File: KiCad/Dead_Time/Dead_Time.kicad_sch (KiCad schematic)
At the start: 13 parts, among them Q7 PNP_BC558, U1 L272M, U2 74AUC2G04

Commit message: alla pcber er klar til routing
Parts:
- removed U1: L272M, Package_DIP:DIP-8_W7.62mm_LongPads, symbol Amplifier_Operational:L272M
- removed U2: 74AUC2G04, Package_DIP:DIP-14_W7.62mm, symbol 74xGxx:74AUC2G04
- added U1: 74AUC2G04, Package_DIP:DIP-14_W7.62mm, symbol 74xGxx:74AUC2G04
- added U2: Opamp_Dual, Package_DIP:DIP-8_W7.62mm, symbol Device:Opamp_Dual
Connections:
- net +5V: now also U1.5 (VCC)
- net GND: now also U1.2 (GND)
- net Meas_VStep1: now also U2.2 (-)
- net Meas_VStep2: now also U2.5 (+)
- net PWM1: now also U1.1, U2.1
- net PWM1_NOT: now also U1.6
- net PWM2: now also U1.3, U2.7
- net PWM2_NOT: now also U1.4
- net at C3.1, R9.2: now also U2.3 (+), U2.6 (-)

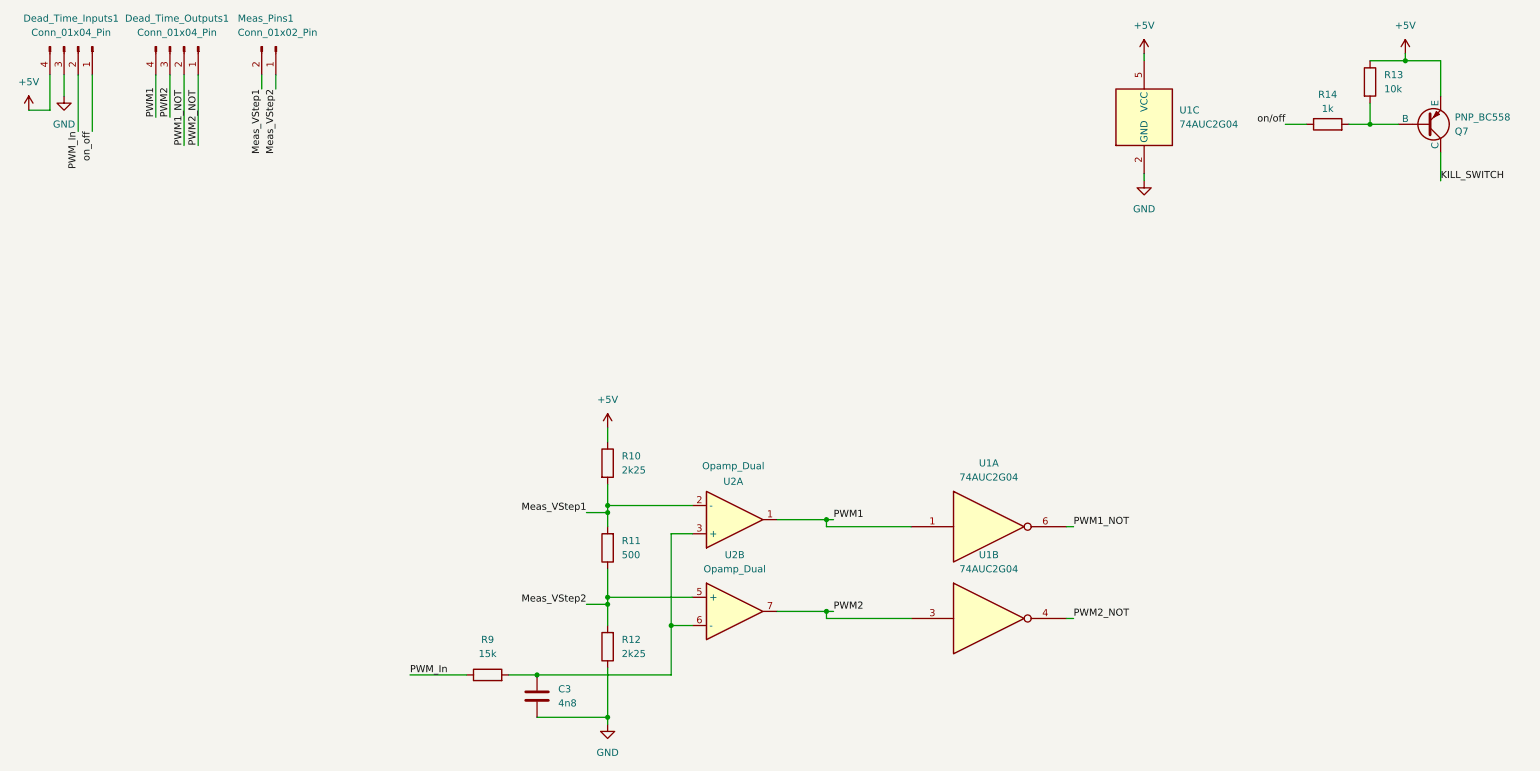
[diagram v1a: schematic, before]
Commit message: deadtime pcb almost done, missing 1 gnd connection
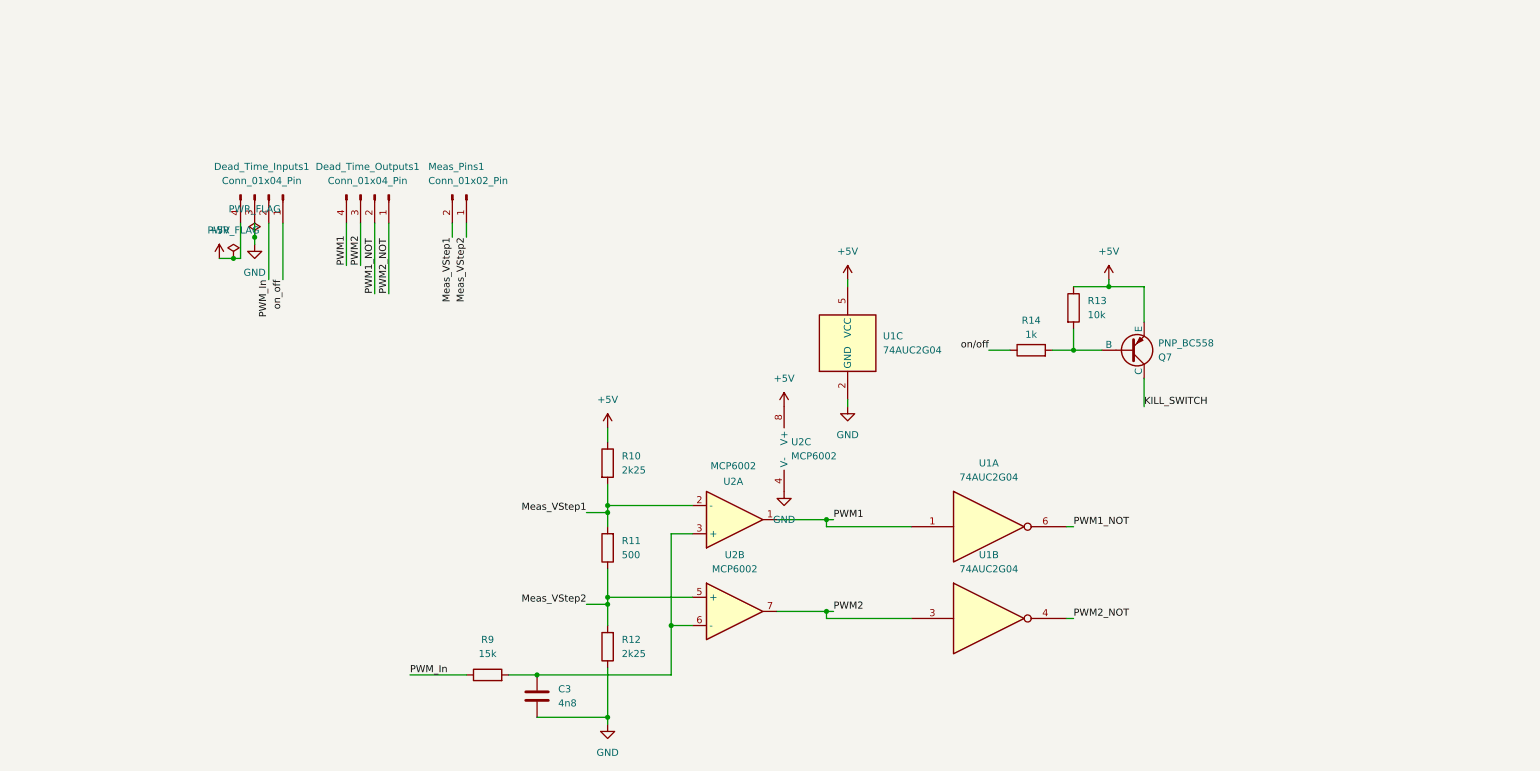
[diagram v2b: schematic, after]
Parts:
- added unit 3 of U2
- U2: value Opamp_Dual -> MCP6002
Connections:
- net +5V: now also U2.8 (V+)
- net GND: now also U2.4 (V-)
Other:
- moved on the sheet: Dead_Time_Inputs1, Dead_Time_Outputs1, Meas_Pins1, Q7, R13, R14, U1C

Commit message: gemme punkt før jeg laver om i deadtime pcb
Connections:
- net +5V: no longer U2.8 (V+)
- net KILL_SWITCH: now also U2.8 (V+)
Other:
- moved on the sheet: Dead_Time_Inputs1, Dead_Time_Outputs1, Meas_Pins1, Q7, R13, R14, U1C, U2C

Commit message: pcb layouts done
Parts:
- removed Meas_Pins1: Conn_01x02_Pin, Connector_PinHeader_2.54mm:PinHeader_1x02_P2.54mm_Vertical, symbol Connector:Conn_01x02_Pin
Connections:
- net Meas_VStep1: no longer names the net of R10.2, R11.2, U2.2 (-)
- net Meas_VStep2: no longer names the net of R11.1, R12.2, U2.5 (+)
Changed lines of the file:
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@@
 	(paper "A4")
-	(junction
-		(at 118.11 102.87)
-		(diameter 0)
-		(color 0 0 0 0)
-	)
 	(junction
 		(at 118.11 118.11)
@@
 	)
 	(junction
-		(at 118.11 119.38)
-		(diameter 0)
-		(color 0 0 0 0)
-	)
-	(junction
 		(at 256.54 31.75)
 		(diameter 0)
@@
 	(wire
 		(pts
-			(xy 114.3 119.38) (xy 118.11 119.38)
-		)
-		(stroke
-			(width 0)
-			(type default)
-		)
-	)
-	(wire
-		(pts
 			(xy 200.66 105.41) (xy 201.93 105.41)
 		)
@@
 	(wire
 		(pts
-			(xy 118.11 102.87) (xy 118.11 105.41)
+			(xy 118.11 101.6) (xy 118.11 105.41)
 		)
 		(stroke
@@
 	(wire
 		(pts
-			(xy 114.3 102.87) (xy 118.11 102.87)
-		)
-		(stroke
-			(width 0)
-			(type default)
-		)
-	)
-	(wire
-		(pts
 			(xy 200.66 121.92) (xy 201.93 121.92)
 		)
@@
 	(wire
 		(pts
-			(xy 68.58 24.13) (xy 68.58 26.67)
-		)
-		(stroke
-			(width 0)
-			(type default)
-		)
-	)
-	(wire
-		(pts
 			(xy 82.55 132.08) (xy 92.71 132.08)
 		)
@@
 	(wire
 		(pts
-			(xy 66.04 24.13) (xy 66.04 26.67)
-		)
-		(stroke
-			(width 0)
-			(type default)
-		)
-	)
-	(wire
-		(pts
 			(xy 105.41 132.08) (xy 129.54 132.08)
 		)
@@
 	(wire
 		(pts
-			(xy 118.11 101.6) (xy 118.11 102.87)
-		)
-		(stroke
-			(width 0)
-			(type default)
-		)
-	)
-	(wire
-		(pts
 			(xy 256.54 31.75) (xy 256.54 27.94)
 		)
@@
 	(wire
 		(pts
-			(xy 118.11 118.11) (xy 118.11 119.38)
-		)
-		(stroke
-			(width 0)
-			(type default)
-		)
-	)
-	(wire
-		(pts
 			(xy 262.89 19.05) (xy 262.89 20.32)
 		)
@@
 	(wire
 		(pts
-			(xy 118.11 119.38) (xy 118.11 123.19)
+			(xy 118.11 118.11) (xy 118.11 123.19)
 		)
 		(stroke
@@
 		)
 	)
-	(label "Meas_VStep1"
-		(at 66.04 26.67 270)
-		(effects
-			(font
-				(size 1.27 1.27)
-			)
-			(justify right bottom)
-		)
-	)
 	(label "PWM1"
 		(at 158.75 104.14 0)
@@
 		)
 	)
-	(label "Meas_VStep2"
-		(at 68.58 26.67 270)
-		(effects
-			(font
-				(size 1.27 1.27)
-			)
-			(justify right bottom)
-		)
-	)
-	(label "Meas_VStep2"
-		(at 114.3 119.38 180)
-		(effects
-			(font
-				(size 1.27 1.27)
-			)
-			(justify right bottom)
-		)
-	)
 	(label "PWM1_NOT"
 		(at 201.93 105.41 0)
@@
 			)
 			(justify left bottom)
-		)
-	)
-	(label "Meas_VStep1"
-		(at 114.3 102.87 180)
-		(effects
-			(font
-				(size 1.27 1.27)
-			)
-			(justify right bottom)
 		)
 	)
@@
 					(unit 1)
 				)
-			)
-		)
-	)
-	(symbol
-		(lib_id "Connector:Conn_01x02_Pin")
-		(at 68.58 19.05 270)
-		(unit 1)
-		(exclude_from_sim no)
-		(in_bom yes)
-		(on_board yes)
-		(dnp no)
-		(property "Reference" "Meas_Pins1"
-			(at 61.722 13.97 90)
-			(effects
-				(font
-					(size 1.27 1.27)
-				)
-				(justify left)
-			)
-		)
-		(property "Value" "Conn_01x02_Pin"
-			(at 61.722 16.51 90)
-			(effects
-				(font
-					(size 1.27 1.27)
-				)
-				(justify left)
-			)
-		)
-		(property "Footprint" "Connector_PinHeader_2.54mm:PinHeader_1x02_P2.54mm_Vertical"
-			(at 68.58 19.05 0)
-			(effects
-				(font
-					(size 1.27 1.27)
-				)
-				(hide yes)
-			)
-		)
-		(property "Datasheet" "~"
-			(at 68.58 19.05 0)
-			(effects
-				(font
-					(size 1.27 1.27)
-				)
-				(hide yes)
-			)
-		)
-		(property "Description" "Generic connector, single row, 01x02, script generated"
-			(at 68.58 19.05 0)
-			(effects
-				(font
-					(size 1.27 1.27)
-				)
-				(hide yes)
-			)
-		)
-		(pin "2"
-		)
-		(pin "1"
-		)
-		(instances
-			(project "Metaldetector"
-				(path "/1ff50a95-4e06-4ec7-aaf8-e1c2108289fd/6213d659-1224-4e09-b0ce-067080e6a783"
-					(reference "Meas_Pins1")
-					(unit 1)
-				)
-			)
-			(project ""
-				(path "/a29309b2-6eea-428f-846f-19d18e25e7df"
-					(reference "Meas_Pins1")
-					(unit 1)
-				)
